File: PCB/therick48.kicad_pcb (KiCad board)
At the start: 2 copper layers, 226.5 x 75.8 mm, 125 parts, among them J1 TYPE-C-31-M12_13, J2 AVR-ISP-6, K1 KEYSW, K10 KEYSW, K11 KEYSW, K12 KEYSW, K13 KEYSW, K14 KEYSW, K15 KEYSW, K16 KEYSW, K17 KEYSW, K18 KEYSW, K19 KEYSW, K2 KEYSW, K20 KEYSW, K21 KEYSW, K22 KEYSW, K23 KEYSW, K24 KEYSW, K25 KEYSW, K26 KEYSW, K27 KEYSW, K28 KEYSW, K29 KEYSW, K3 KEYSW, K30 KEYSW, K31 KEYSW, K32 KEYSW, K33 KEYSW, K34 KEYSW, K35 KEYSW, K36 KEYSW, K37 KEYSW, K38 KEYSW, K39 KEYSW, K4 KEYSW, K40 KEYSW, K41 KEYSW, K42 KEYSW, K43 KEYSW, K44 KEYSW, K45 KEYSW, K46 KEYSW, K47 KEYSW, K48 KEYSW, K5 KEYSW, K6 KEYSW, K7 KEYSW, K8 KEYSW, K9 KEYSW, SW1 SW_PUSH, U1 ATMEGA32U4, U2 HOLE, U3 USBLC6-2SC6, U8 HOLE, Y1 16MHz

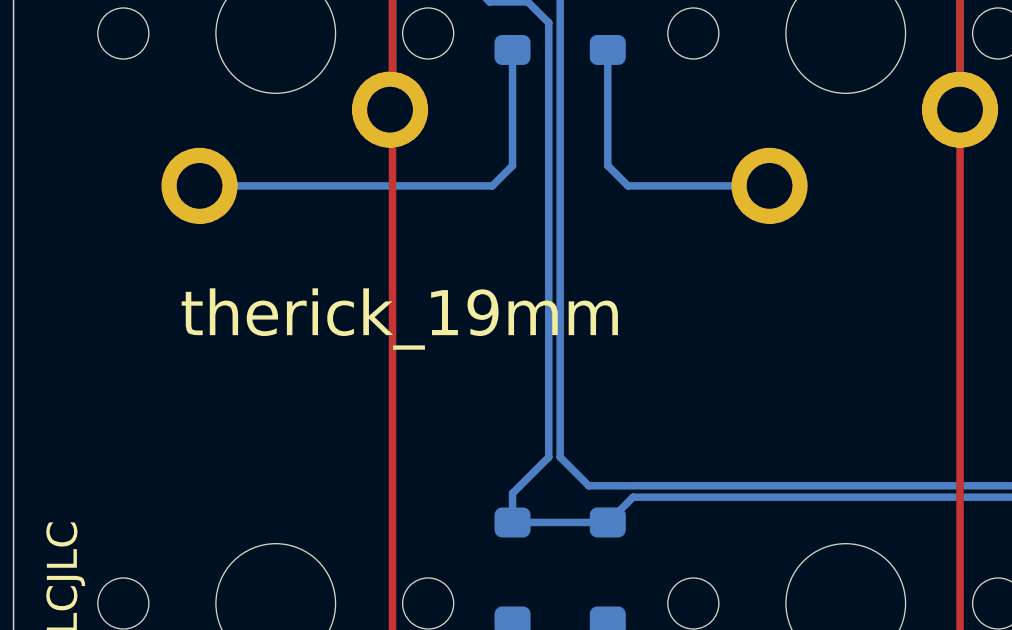
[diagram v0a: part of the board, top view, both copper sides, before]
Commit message: Align Switches
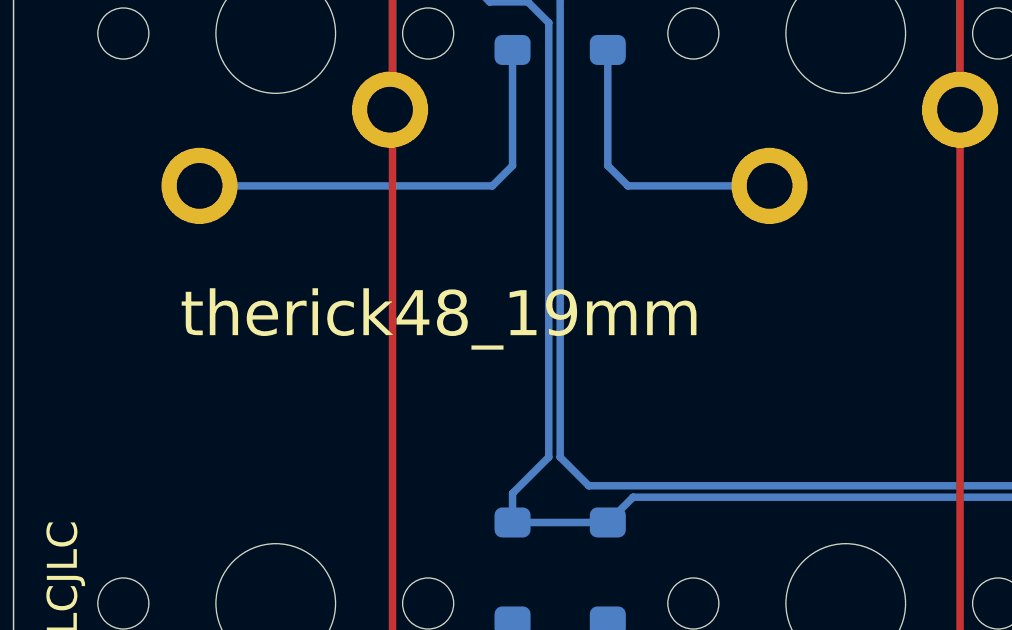
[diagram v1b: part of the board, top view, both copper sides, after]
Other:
- board text added: "therick48_19mm"
- board text removed: "therick_19mm"
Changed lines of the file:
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@@
     (46 B.CrtYd user)
     (47 F.CrtYd user)
-    (48 B.Fab user hide)
+    (48 B.Fab user)
     (49 F.Fab user)
   )
@@
     (solder_mask_min_width 0.25)
     (aux_axis_origin 160.005 72.985)
-    (visible_elements 7FFFEFFF)
+    (visible_elements 7FFFFFFF)
     (pcbplotparams
       (layerselection 0x010fc_ffffffff)
@@
     )
   )
-  (gr_text therick_19mm (at 52.288143 91.821) (layer F.SilkS)
+  (gr_text therick48_19mm (at 52.288143 91.821) (layer F.SilkS)
     (effects (font (size 1.5 1.5) (thickness 0.2)) (justify left))
   )

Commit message: Add Gerbers
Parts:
- removed U8: HOLE, Artwork:QMKBadgeSmall
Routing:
- net Net-(D37-Pad2): track 21.9 -> 14.3 mm
- net XTAL2: track 18.4 -> 11.7 mm
- net VCC: track 144.7 -> 151.1 mm, vias 2 -> 6
- net col2: track 77.5 -> 74.9 mm
- net col1: track 63.1 -> 65.4 mm
- net col8: track 198.7 -> 197.9 mm
- net row1: track 204.3 -> 204.8 mm
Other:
- board text added: "PCB Rev 1.0"
- board text added: "therick48"
- board text removed: "therick"
- board text removed: "therick48_19mm"

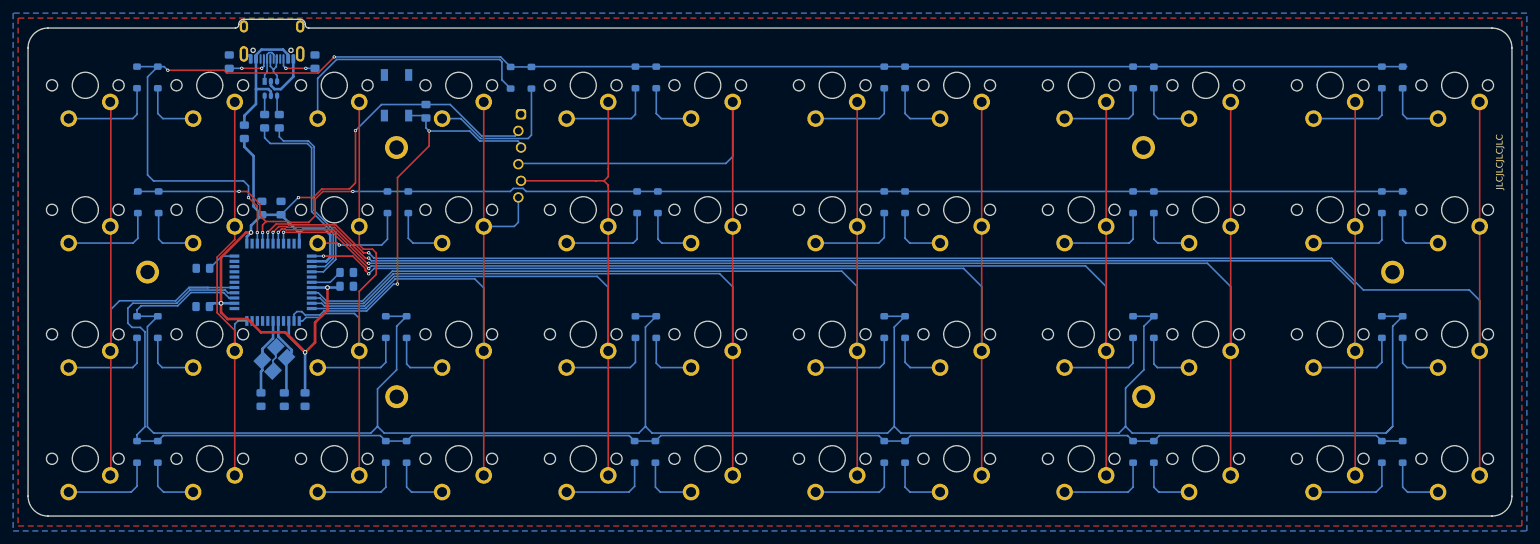
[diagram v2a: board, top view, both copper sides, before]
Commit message: Changed pins to make routing cleaner
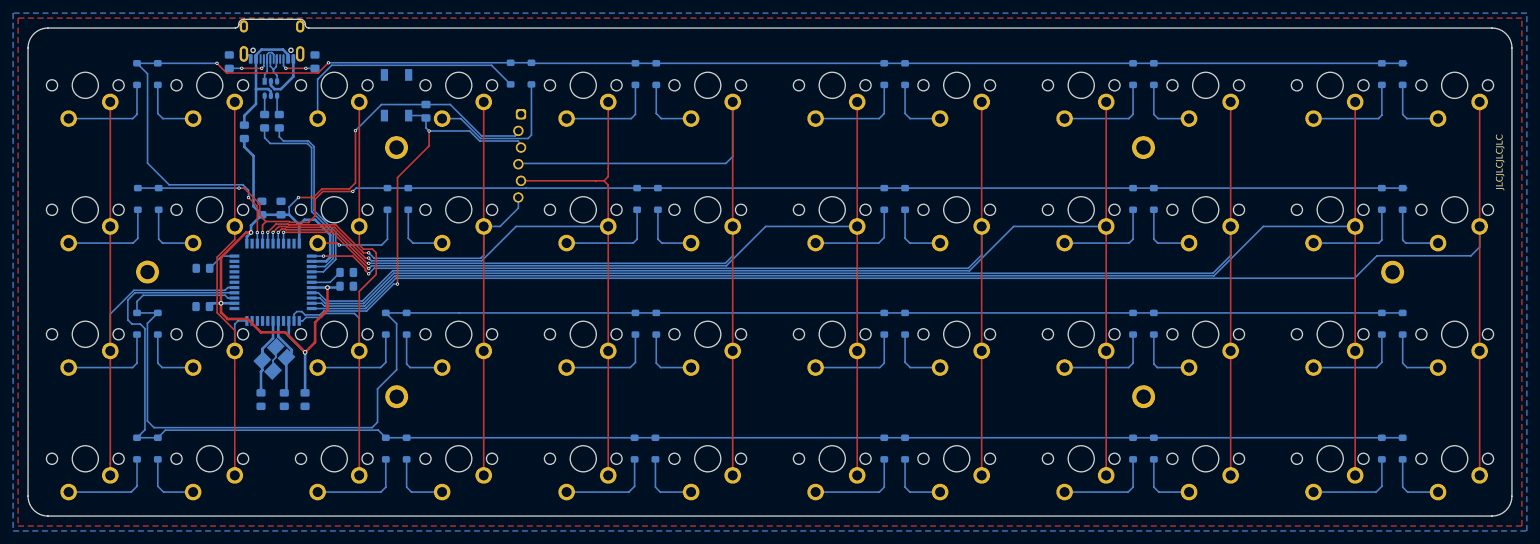
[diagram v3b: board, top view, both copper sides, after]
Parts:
- moved D3 0.64 mm to (120.4, 42.7)
- moved D4 0.64 mm to (123.6, 42.7)
- moved D13 0.51 mm to (63.5, 61.8)
- moved D14 0.51 mm to (66.7, 61.8)
- moved D15 0.51 mm to (101.6, 61.8)
- moved D16 0.51 mm to (104.8, 61.8)
- moved D17 0.51 mm to (139.7, 61.8)
- moved D18 0.51 mm to (142.9, 61.8)
- moved D19 0.51 mm to (177.4, 61.8)
- moved D20 0.51 mm to (180.6, 61.8)
- moved D21 0.51 mm to (215.4, 61.8)
- moved D22 0.51 mm to (218.6, 61.8)
- moved D23 0.51 mm to (253.4, 61.8)
- moved D24 0.51 mm to (256.5, 61.8)
- moved D1 0.51 mm to (63.4, 42.8)
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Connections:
- U1 pad 10: col4 -> col10
- U1 pad 11: col3 -> col11
- U1 pad 38: col11 -> col3
- U1 pad 39: col10 -> col4
- U1 pad 40: col9 -> col5
- U1 pad 41: col8 -> col6
- U1 pad 8: col6 -> col8
- U1 pad 9: col5 -> col9
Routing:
- net row2: track 338.9 -> 247.2 mm
- net col10: track 238.0 -> 221.5 mm, vias 2 -> 0
- net col11: track 256.8 -> 242.3 mm, vias 2 -> 0
- net col8: track 197.9 -> 183.5 mm, vias 2 -> 0
- net col9: track 217.8 -> 205.1 mm, vias 2 -> 0
- net col7: track 171.8 -> 166.1 mm
- net col0: track 86.8 -> 83.3 mm
- net Net-(D3-Pad2): track 40.2 -> 37.5 mm
- net row3: track 236.8 -> 234.2 mm
- net col3: track 104.6 -> 107.0 mm, vias 0 -> 2
- net col6: track 153.5 -> 151.2 mm, vias 0 -> 2
- net row0: track 238.0 -> 236.4 mm
- net col5: track 175.2 -> 176.5 mm, vias 0 -> 2
- net VCC: track 151.1 -> 151.9 mm
- net row1: track 204.8 -> 204.1 mm
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
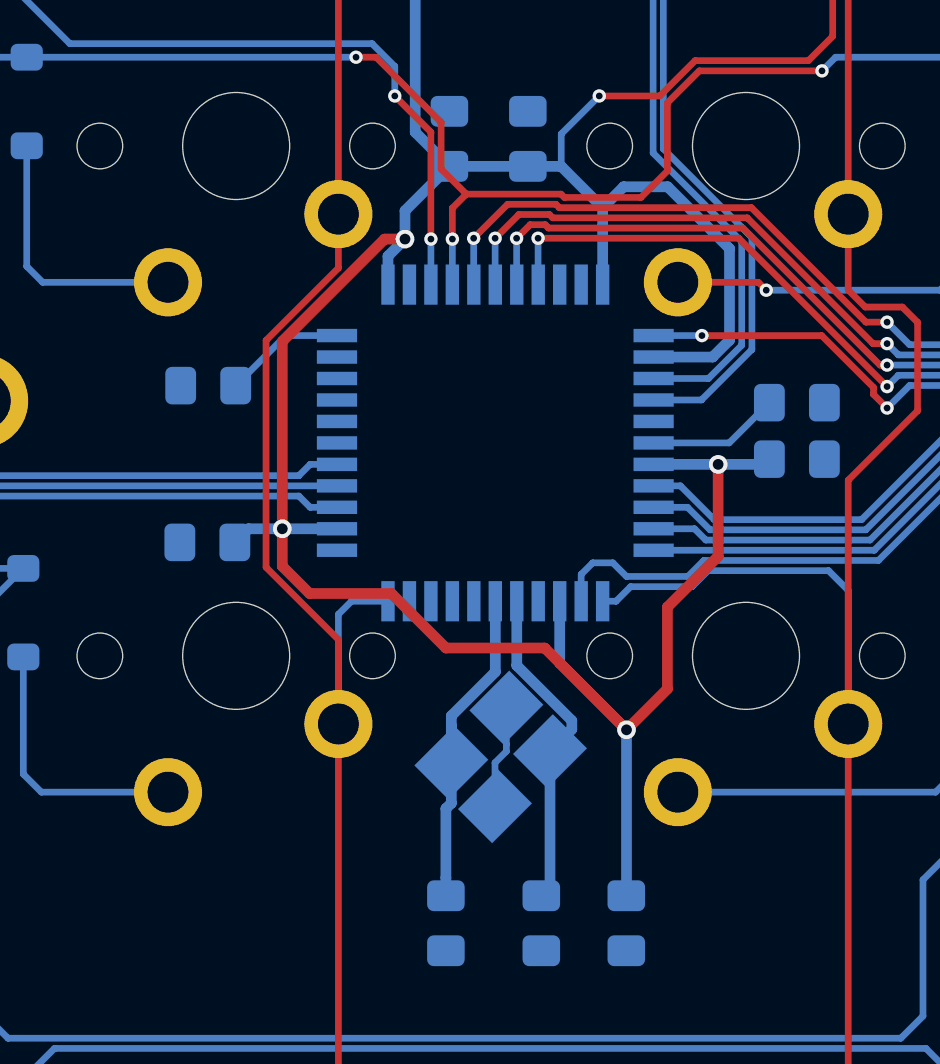
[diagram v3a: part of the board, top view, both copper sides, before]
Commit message: Made capacitors effective
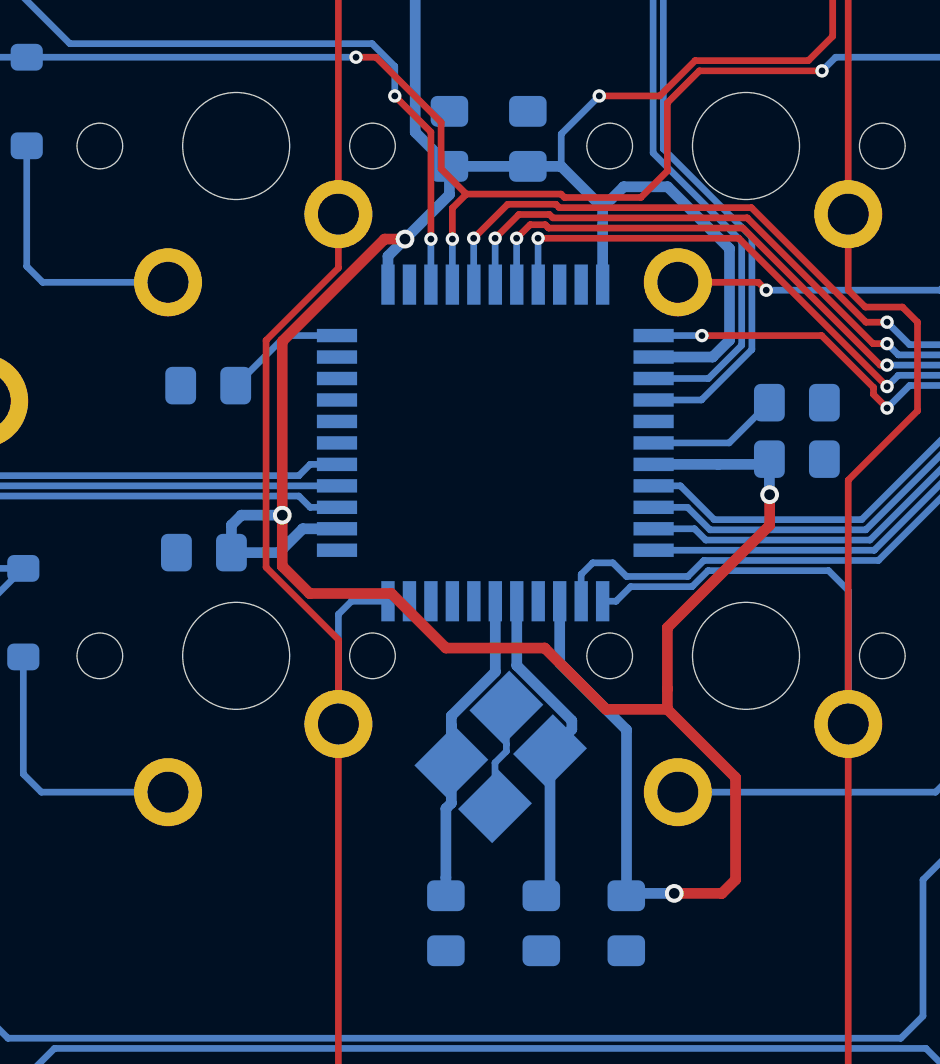
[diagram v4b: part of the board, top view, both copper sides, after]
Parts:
- moved C2 17.9 mm to (73.3, 78.6), turned to 180 degrees
- moved C5 17.5 mm to (82.4, 63.2), turned to 90 degrees
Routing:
- net VCC: track 151.9 -> 167.7 mm
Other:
- board text added: "PCB Rev 1.1"
- board text removed: "100nF"
- board text removed: "10K"
- board text removed: "10uF"
- board text removed: "16MHz"
- board text removed: "1uF"
- board text removed: "22"
- board text removed: "22pF"
- board text removed: "5.1K"
- board text removed: "500mA"
- board text removed: "PCB Rev 1.0"
